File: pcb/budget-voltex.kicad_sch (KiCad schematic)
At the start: 10 parts

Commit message: put elements on pcb
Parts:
- BT-A1: renamed from BT-A; footprint (none) -> Button_Switch_Keyboard:SW_Cherry_MX_1.00u_PCB
- BT-B1: renamed from BT-B; footprint (none) -> Button_Switch_Keyboard:SW_Cherry_MX_1.00u_PCB
- BT-C1: renamed from BT-C; footprint (none) -> Button_Switch_Keyboard:SW_Cherry_MX_1.00u_PCB
- BT-D1: renamed from BT-D; footprint (none) -> Button_Switch_Keyboard:SW_Cherry_MX_1.00u_PCB
- FX-L1: renamed from FX-L; footprint (none) -> Button_Switch_Keyboard:SW_Cherry_MX_1.00u_PCB
- FX-R1: renamed from FX-R; footprint (none) -> Button_Switch_Keyboard:SW_Cherry_MX_1.00u_PCB
- Start1: renamed from Start; footprint (none) -> Button_Switch_Keyboard:SW_Cherry_MX_1.00u_PCB
- renumbered KnobL to KnobL1, KnobR to KnobR1
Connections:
- net SDA: now reaches KnobL1.1 (SCL), KnobR1.1 (SCL)
- net SDA: now also A1.1 (GPIO0)
- net SCL: now reaches KnobL1.6 (SDA), KnobR1.6 (SDA)
- net SCL: now also A1.2 (GPIO1)
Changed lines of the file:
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@@
 	(paper "A4")
+	(junction
+		(at 182.88 77.47)
+		(diameter 0)
+		(color 0 0 0 0)
+	)
 	(junction
 		(at 76.2 157.48)
@@
 	)
 	(junction
+		(at 179.07 71.12)
+		(diameter 0)
+		(color 0 0 0 0)
+	)
+	(junction
 		(at 106.68 157.48)
 		(diameter 0)
@@
 	(wire
 		(pts
+			(xy 179.07 71.12) (xy 189.23 71.12)
+		)
+		(stroke
+			(width 0)
+			(type default)
+		)
+	)
+	(wire
+		(pts
 			(xy 92.71 113.03) (xy 92.71 105.41)
 		)
@@
 	(wire
 		(pts
+			(xy 179.07 71.12) (xy 179.07 63.5)
+		)
+		(stroke
+			(width 0)
+			(type default)
+		)
+	)
+	(wire
+		(pts
 			(xy 83.82 157.48) (xy 83.82 146.05)
 		)
@@
 	(wire
 		(pts
+			(xy 182.88 77.47) (xy 182.88 66.04)
+		)
+		(stroke
+			(width 0)
+			(type default)
+		)
+	)
+	(wire
+		(pts
 			(xy 82.55 105.41) (xy 82.55 120.65)
 		)
@@
 	(wire
 		(pts
-			(xy 182.88 91.44) (xy 182.88 66.04)
+			(xy 182.88 91.44) (xy 182.88 77.47)
 		)
 		(stroke
@@
 	(wire
 		(pts
-			(xy 179.07 88.9) (xy 179.07 63.5)
+			(xy 179.07 88.9) (xy 179.07 71.12)
 		)
 		(stroke
@@
 	(wire
 		(pts
+			(xy 182.88 77.47) (xy 190.5 77.47)
+		)
+		(stroke
+			(width 0)
+			(type default)
+		)
+	)
+	(wire
+		(pts
 			(xy 100.33 115.57) (xy 90.17 115.57)
 		)
@@
 			(width 0)
 			(type default)
+		)
+	)
+	(global_label "SCL"
+		(shape input)
+		(at 74.93 105.41 270)
+		(fields_autoplaced yes)
+		(effects
+			(font
+				(size 1.27 1.27)
+			)
+			(justify right)
+		)
+		(property "Intersheetrefs" "${INTERSHEET_REFS}"
+			(at 74.93 111.9028 90)
+			(effects
+				(font
+					(size 1.27 1.27)
+				)
+				(justify right)
+				(hide yes)
+			)
+		)
+	)
+	(global_label "SCL"
+		(shape input)
+		(at 190.5 77.47 0)
+		(fields_autoplaced yes)
+		(effects
+			(font
+				(size 1.27 1.27)
+			)
+			(justify left)
+		)
+		(property "Intersheetrefs" "${INTERSHEET_REFS}"
+			(at 196.9928 77.47 0)
+			(effects
+				(font
+					(size 1.27 1.27)
+				)
+				(justify left)
+				(hide yes)
+			)
+		)
+	)
+	(global_label "SDA"
+		(shape input)
+		(at 72.39 105.41 270)
+		(fields_autoplaced yes)
+		(effects
+			(font
+				(size 1.27 1.27)
+			)
+			(justify right)
+		)
+		(property "Intersheetrefs" "${INTERSHEET_REFS}"
+			(at 72.39 111.9633 90)
+			(effects
+				(font
+					(size 1.27 1.27)
+				)
+				(justify right)
+				(hide yes)
+			)
+		)
+	)
+	(global_label "SDA"
+		(shape input)
+		(at 189.23 71.12 0)
+		(fields_autoplaced yes)
+		(effects
+			(font
+				(size 1.27 1.27)
+			)
+			(justify left)
+		)
+		(property "Intersheetrefs" "${INTERSHEET_REFS}"
+			(at 195.7833 71.12 0)
+			(effects
+				(font
+					(size 1.27 1.27)
+				)
+				(justify left)
+				(hide yes)
+			)
 		)
 	)
@@
 		(dnp no)
 		(fields_autoplaced yes)
-		(property "Reference" "KnobL"
+		(property "Reference" "KnobL1"
 			(at 158.75 53.34 0)
 			(effects
@@
 			(project "sdvx-slim"
 				(path "/f61fff6d-f3d6-4025-b479-f6b910efe925"
-					(reference "KnobL")
+					(reference "KnobL1")
 					(unit 1)
 				)
@@
 		(on_board yes)
 		(dnp no)
-		(property "Reference" "FX-L"
+		(property "Reference" "FX-L1"
 			(at 82.55 152.4 0)
 			(effects
@@
 			)
 		)
-		(property "Footprint" ""
+		(property "Footprint" "Button_Switch_Keyboard:SW_Cherry_MX_1.00u_PCB"
 			(at 76.2 152.4 0)
 			(effects
@@
 			(project "sdvx-slim"
 				(path "/f61fff6d-f3d6-4025-b479-f6b910efe925"
-					(reference "FX-L")
+					(reference "FX-L1")
 					(unit 1)
 				)
@@
 		(dnp no)
 		(fields_autoplaced yes)
-		(property "Reference" "Start"
+		(property "Reference" "Start1"
 			(at 95.25 125.7299 90)
 			(effects
@@
 			)
 		)
-		(property "Footprint" ""
+		(property "Footprint" "Button_Switch_Keyboard:SW_Cherry_MX_1.00u_PCB"
 			(at 92.71 127 0)
 			(effects
@@
 			(project "sdvx-slim"
 				(path "/f61fff6d-f3d6-4025-b479-f6b910efe925"
-					(reference "Start")
+					(reference "Start1")
 					(unit 1)
 				)
@@
 		(dnp no)
 		(fields_autoplaced yes)
-		(property "Reference" "BT-D"
+		(property "Reference" "BT-D1"
 			(at 116.84 139.6999 90)
 			(effects
@@
 			)
 		)
-		(property "Footprint" ""
+		(property "Footprint" "Button_Switch_Keyboard:SW_Cherry_MX_1.00u_PCB"
 			(at 114.3 140.97 0)
 			(effects
@@
 			(project "sdvx-slim"
 				(path "/f61fff6d-f3d6-4025-b479-f6b910efe925"
-					(reference "BT-D")
+					(reference "BT-D1")
 					(unit 1)
 				)
@@
 		(dnp no)
 		(fields_autoplaced yes)
-		(property "Reference" "KnobR"
+		(property "Reference" "KnobR1"
 			(at 158.75 78.74 0)
 			(effects
@@
 			(project ""
 				(path "/f61fff6d-f3d6-4025-b479-f6b910efe925"
-					(reference "KnobR")
+					(reference "KnobR1")
 					(unit 1)
 				)
@@
 		(dnp no)
 		(fields_autoplaced yes)
-		(property "Reference" "BT-A"
+		(property "Reference" "BT-A1"
 			(at 71.12 139.6999 90)
 			(effects
@@
 			)
 		)
-		(property "Footprint" ""
+		(property "Footprint" "Button_Switch_Keyboard:SW_Cherry_MX_1.00u_PCB"
 			(at 68.58 140.97 0)
 			(effects
@@
 			(project ""
 				(path "/f61fff6d-f3d6-4025-b479-f6b910efe925"
-					(reference "BT-A")
+					(reference "BT-A1")
 					(unit 1)
 				)
@@
 		(dnp no)
 		(fields_autoplaced yes)
-		(property "Reference" "BT-C"
+		(property "Reference" "BT-C1"
 			(at 102.87 139.6999 90)
 			(effects
@@
 			)
 		)
-		(property "Footprint" ""
+		(property "Footprint" "Button_Switch_Keyboard:SW_Cherry_MX_1.00u_PCB"
 			(at 100.33 140.97 0)
 			(effects
@@
 			(project "sdvx-slim"
 				(path "/f61fff6d-f3d6-4025-b479-f6b910efe925"
-					(reference "BT-C")
+					(reference "BT-C1")
 					(unit 1)
 				)
@@
 		(dnp no)
 		(fields_autoplaced yes)
-		(property "Reference" "BT-B"
+		(property "Reference" "BT-B1"
 			(at 86.36 139.6999 90)
 			(effects
@@
 			)
 		)
-		(property "Footprint" ""
+		(property "Footprint" "Button_Switch_Keyboard:SW_Cherry_MX_1.00u_PCB"
 			(at 83.82 140.97 0)
 			(effects
@@
 			(project "sdvx-slim"
 				(path "/f61fff6d-f3d6-4025-b479-f6b910efe925"
-					(reference "BT-B")
+					(reference "BT-B1")
 					(unit 1)
 				)
@@
 		(dnp no)
 		(fields_autoplaced yes)
-		(property "Reference" "FX-R"
+		(property "Reference" "FX-R1"
 			(at 109.22 151.1299 90)
 			(effects
@@
 			)
 		)
-		(property "Footprint" ""
+		(property "Footprint" "Button_Switch_Keyboard:SW_Cherry_MX_1.00u_PCB"
 			(at 106.68 152.4 0)
 			(effects
@@
 			(project "sdvx-slim"
 				(path "/f61fff6d-f3d6-4025-b479-f6b910efe925"
-					(reference "FX-R")
+					(reference "FX-R1")
 					(unit 1)
 				)

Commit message: finish schematic, finish wiring for pcb
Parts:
- added R1, R2, R3, R4: 5K1, Resistor_SMD:R_0603_1608Metric_Pad0.98x0.95mm_HandSolder, symbol Device:R_Small
- added USB1: HRO-TYPE-C-31-M-12, Type-C:HRO-TYPE-C-31-M-12-HandSoldering, symbol Type-C:HRO-TYPE-C-31-M-12
- A1: footprint Module:RaspberryPi_Pico_SMD_HandSolder -> Module:RaspberryPi_Pico_SMD; symbol MCU_Module:RaspberryPi_Pico_Debug -> MCU_Module:RaspberryPi_Pico_Extensive
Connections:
- net GND: now also BT-A1.2 (B), BT-B1.2 (B), BT-C1.2 (B), BT-D1.2 (B), FX-L1.2 (B), FX-R1.2 (B), Start1.2 (B), R3.2, R4.2, USB1.1 (GND), USB1.12 (GND), USB1.13 (SHIELD)
- net SCL: now also R2.2
- net SDA: now also R1.2
- net +3V3: now reaches A1.36 (3V3)
- net +3V3: now also R1.1, R2.1
- net at A1.40 (VBUS): now also USB1.11 (VBUS), USB1.2 (VBUS)
- new net: A1.TP2 (USB_DM), USB1.5 (DN2), USB1.7 (DN1)
- new net: A1.TP3 (USB_DP), USB1.6 (DP1), USB1.8 (DP2)
- new net: R3.1, USB1.4 (CC1)
- new net: R4.1, USB1.10 (CC2)
- no-connect marks 0 -> 4

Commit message: update wiring/schematic, shape pcb
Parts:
- KnobL: renamed from KnobR1; footprint DBV0006A-IPC_A -> TMAG5273A1QDBVR:DBV0006A-IPC_A
- KnobR: renamed from KnobL1; footprint DBV0006A-IPC_A -> TMAG5273A1QDBVR:DBV0006A-IPC_A
- renumbered FX-R1 to FX-L1, FX-L1 to FX-R1, Start1 to Start
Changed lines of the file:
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@@
 		(dnp no)
 		(fields_autoplaced yes)
-		(property "Reference" "KnobL1"
+		(property "Reference" "KnobR"
 			(at 158.75 53.34 0)
 			(effects
@@
 			)
 		)
-		(property "Footprint" "DBV0006A-IPC_A"
+		(property "Footprint" "TMAG5273A1QDBVR:DBV0006A-IPC_A"
 			(at 142.24 63.5 0)
 			(effects
@@
 			(project "sdvx-slim"
 				(path "/f61fff6d-f3d6-4025-b479-f6b910efe925"
-					(reference "KnobL1")
+					(reference "KnobR")
 					(unit 1)
 				)
@@
 		(on_board yes)
 		(dnp no)
-		(property "Reference" "FX-L1"
+		(property "Reference" "FX-R1"
 			(at 82.55 152.4 0)
 			(effects
@@
 			(project "sdvx-slim"
 				(path "/f61fff6d-f3d6-4025-b479-f6b910efe925"
-					(reference "FX-L1")
+					(reference "FX-R1")
 					(unit 1)
 				)
@@
 		(dnp no)
 		(fields_autoplaced yes)
-		(property "Reference" "Start1"
+		(property "Reference" "Start"
 			(at 95.25 125.7299 90)
 			(effects
@@
 			(project "sdvx-slim"
 				(path "/f61fff6d-f3d6-4025-b479-f6b910efe925"
-					(reference "Start1")
+					(reference "Start")
 					(unit 1)
 				)
@@
 		(dnp no)
 		(fields_autoplaced yes)
-		(property "Reference" "KnobR1"
+		(property "Reference" "KnobL"
 			(at 158.75 78.74 0)
 			(effects
@@
 			)
 		)
-		(property "Footprint" "DBV0006A-IPC_A"
+		(property "Footprint" "TMAG5273A1QDBVR:DBV0006A-IPC_A"
 			(at 142.24 88.9 0)
 			(effects
@@
 			(project ""
 				(path "/f61fff6d-f3d6-4025-b479-f6b910efe925"
-					(reference "KnobR1")
+					(reference "KnobL")
 					(unit 1)
 				)
@@
 		(dnp no)
 		(fields_autoplaced yes)
-		(property "Reference" "FX-R1"
+		(property "Reference" "FX-L1"
 			(at 109.22 151.1299 90)
 			(effects
@@
 			(project "sdvx-slim"
 				(path "/f61fff6d-f3d6-4025-b479-f6b910efe925"
-					(reference "FX-R1")
-					(unit 1)
-				)
+					(reference "FX-L1")
+					(unit 1)
+				)

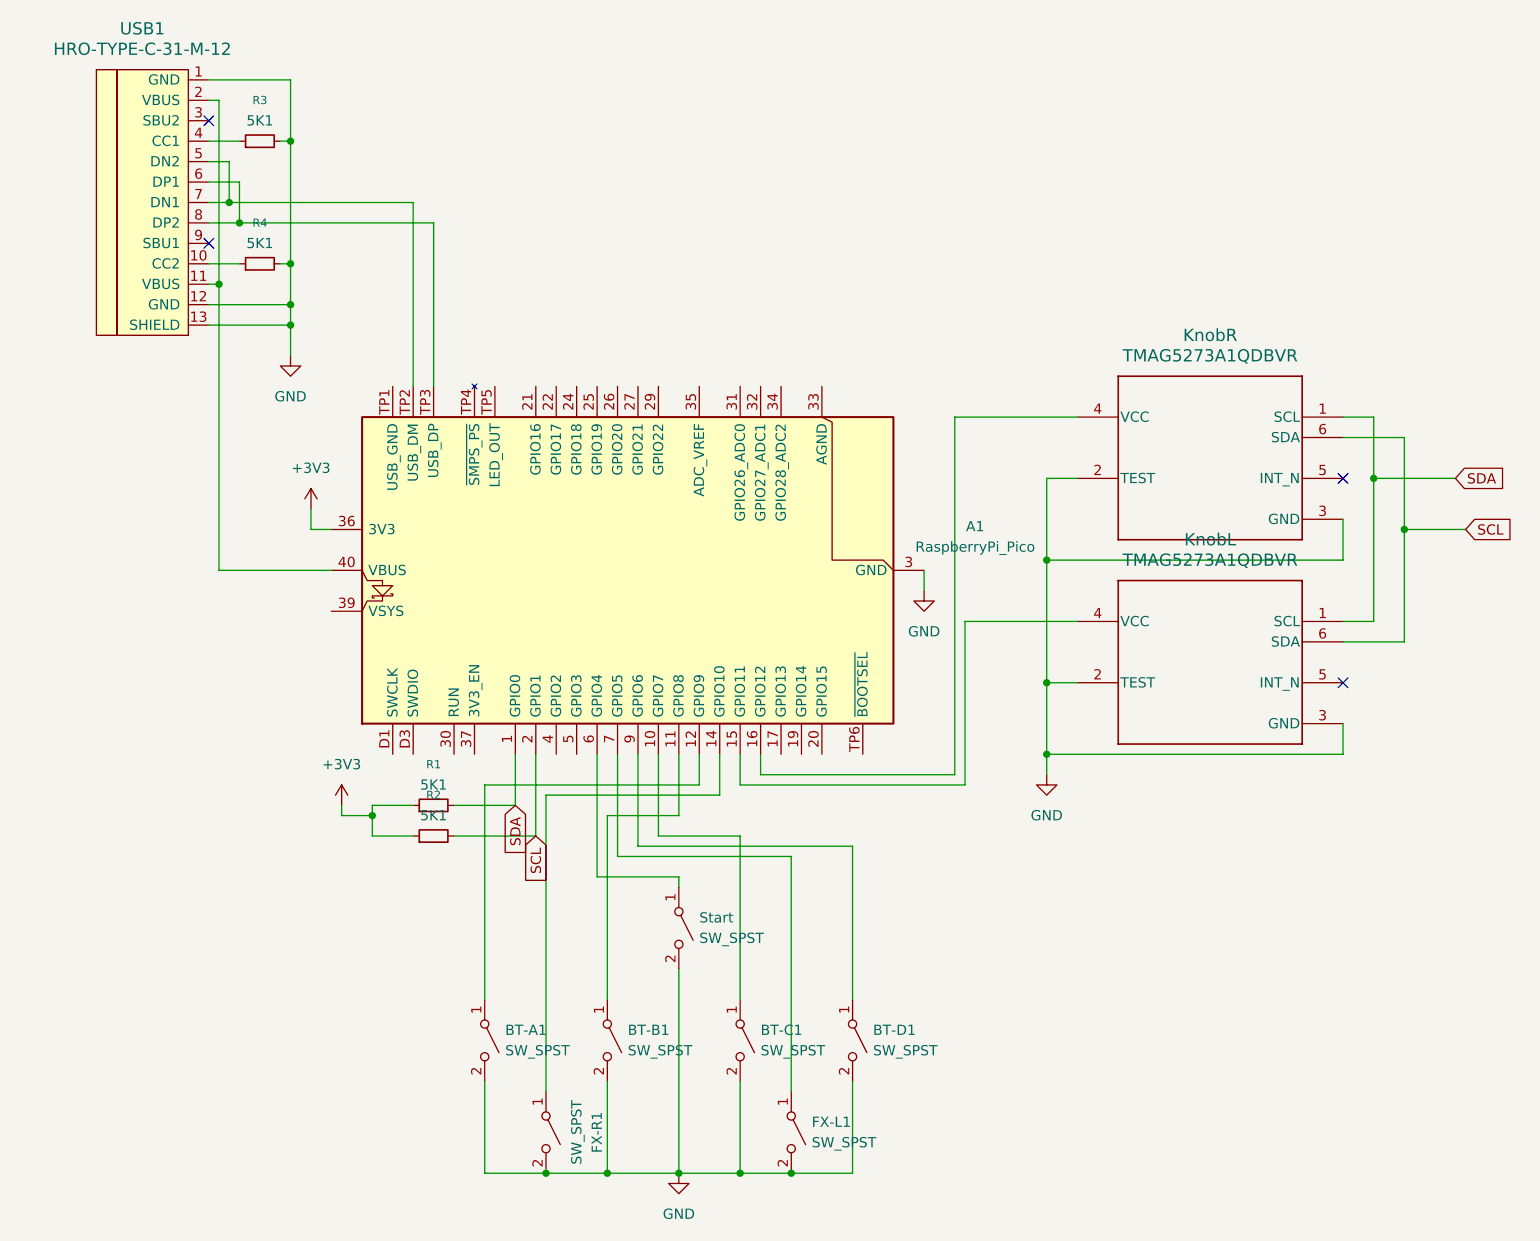
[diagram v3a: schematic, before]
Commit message: Updated key footprints to use chocs, rewire everything
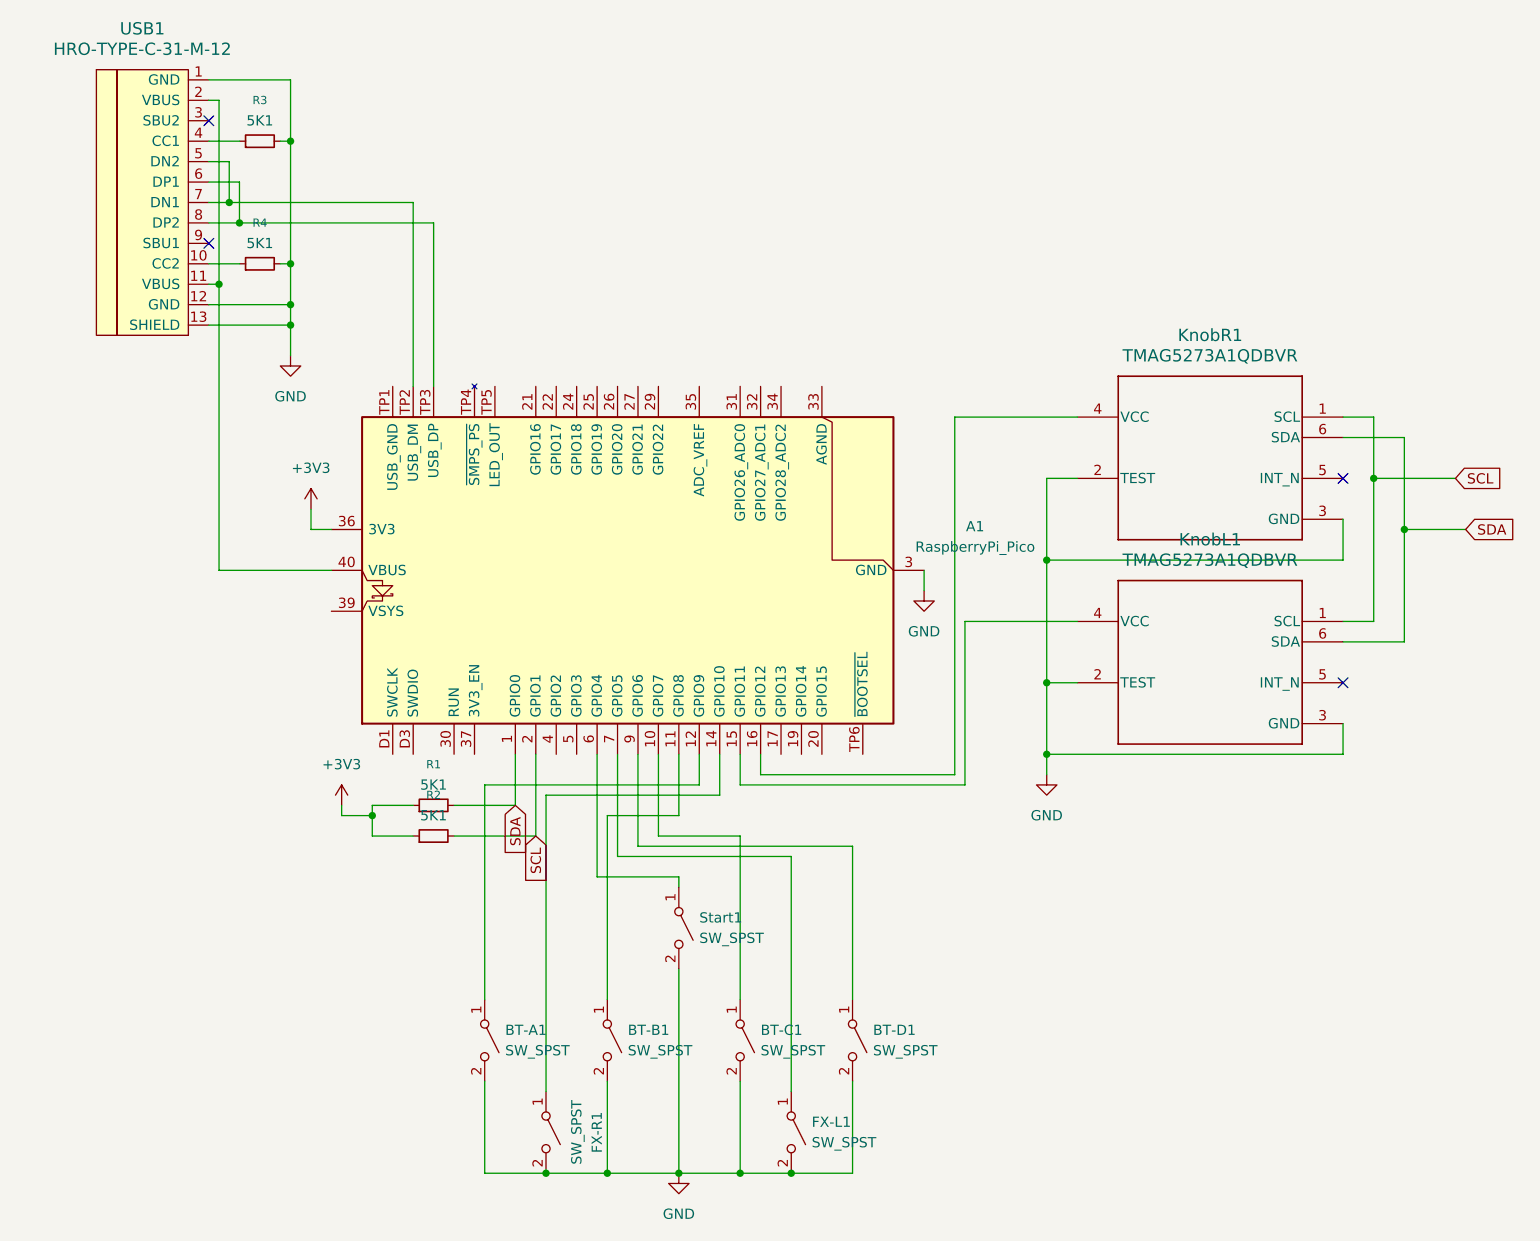
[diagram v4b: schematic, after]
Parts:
- BT-A1, BT-B1, BT-C1, BT-D1, FX-L1, FX-R1: footprint Button_Switch_Keyboard:SW_Cherry_MX_1.00u_PCB -> keyswitches:SW_PG1350
- Start1: renamed from Start; footprint Button_Switch_Keyboard:SW_Cherry_MX_1.00u_PCB -> keyswitches:SW_PG1350
- renumbered KnobL to KnobL1, KnobR to KnobR1
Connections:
- net SCL: now also KnobL1.1 (SCL), KnobR1.1 (SCL); no longer KnobL1.6 (SDA), KnobR1.6 (SDA)
- net SDA: now also KnobL1.6 (SDA), KnobR1.6 (SDA); no longer KnobL1.1 (SCL), KnobR1.1 (SCL)
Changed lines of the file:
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@@
 		)
 	)
-	(global_label "SCL"
+	(global_label "SDA"
 		(shape input)
-		(at 190.5 77.47 0)
+		(at 72.39 111.76 270)
 		(fields_autoplaced yes)
 		(effects
@@
 				(size 1.27 1.27)
 			)
-			(justify left)
+			(justify right)
 		)
 		(property "Intersheetrefs" "${INTERSHEET_REFS}"
-			(at 196.9928 77.47 0)
-			(effects
-				(font
-					(size 1.27 1.27)
-				)
-				(justify left)
-				(hide yes)
-			)
-		)
-	)
-	(global_label "SDA"
+			(at 72.39 118.3133 90)
+			(effects
+				(font
+					(size 1.27 1.27)
+				)
+				(justify right)
+				(hide yes)
+			)
+		)
+	)
+	(global_label "SCL"
 		(shape input)
-		(at 72.39 111.76 270)
+		(at 189.23 71.12 0)
 		(fields_autoplaced yes)
 		(effects
@@
 				(size 1.27 1.27)
 			)
-			(justify right)
+			(justify left)
 		)
 		(property "Intersheetrefs" "${INTERSHEET_REFS}"
-			(at 72.39 118.3133 90)
-			(effects
-				(font
-					(size 1.27 1.27)
-				)
-				(justify right)
+			(at 195.7228 71.12 0)
+			(effects
+				(font
+					(size 1.27 1.27)
+				)
+				(justify left)
 				(hide yes)
 			)
@@
 	(global_label "SDA"
 		(shape input)
-		(at 189.23 71.12 0)
+		(at 190.5 77.47 0)
 		(fields_autoplaced yes)
 		(effects
@@
 		)
 		(property "Intersheetrefs" "${INTERSHEET_REFS}"
-			(at 195.7833 71.12 0)
+			(at 197.0533 77.47 0)
 			(effects
 				(font
@@
 		(dnp no)
 		(fields_autoplaced yes)
-		(property "Reference" "KnobR"
+		(property "Reference" "KnobR1"
 			(at 158.75 53.34 0)
 			(effects
@@
 			(project "sdvx-slim"
 				(path "/f61fff6d-f3d6-4025-b479-f6b910efe925"
-					(reference "KnobR")
+					(reference "KnobR1")
 					(unit 1)
 				)
@@
 			)
 		)
-		(property "Footprint" "Button_Switch_Keyboard:SW_Cherry_MX_1.00u_PCB"
+		(property "Footprint" "keyswitches:SW_PG1350"
 			(at 76.2 152.4 0)
 			(effects
@@
 		(dnp no)
 		(fields_autoplaced yes)
-		(property "Reference" "Start"
+		(property "Reference" "Start1"
 			(at 95.25 125.7299 90)
 			(effects
@@
 			)
 		)
-		(property "Footprint" "Button_Switch_Keyboard:SW_Cherry_MX_1.00u_PCB"
+		(property "Footprint" "keyswitches:SW_PG1350"
 			(at 92.71 127 0)
 			(effects
@@
 			(project "sdvx-slim"
 				(path "/f61fff6d-f3d6-4025-b479-f6b910efe925"
-					(reference "Start")
+					(reference "Start1")
 					(unit 1)
 				)
@@
 			)
 		)
-		(property "Footprint" "Button_Switch_Keyboard:SW_Cherry_MX_1.00u_PCB"
+		(property "Footprint" "keyswitches:SW_PG1350"
 			(at 114.3 140.97 0)
 			(effects
@@
 		(dnp no)
 		(fields_autoplaced yes)
-		(property "Reference" "KnobL"
+		(property "Reference" "KnobL1"
 			(at 158.75 78.74 0)
 			(effects
@@
 			(project ""
 				(path "/f61fff6d-f3d6-4025-b479-f6b910efe925"
-					(reference "KnobL")
+					(reference "KnobL1")
 					(unit 1)
 				)
@@
 			)
 		)
-		(property "Footprint" "Button_Switch_Keyboard:SW_Cherry_MX_1.00u_PCB"
+		(property "Footprint" "keyswitches:SW_PG1350"
 			(at 68.58 140.97 0)
 			(effects
@@
 			)
 		)
-		(property "Footprint" "Button_Switch_Keyboard:SW_Cherry_MX_1.00u_PCB"
+		(property "Footprint" "keyswitches:SW_PG1350"
 			(at 100.33 140.97 0)
 			(effects
@@
 			)
 		)
-		(property "Footprint" "Button_Switch_Keyboard:SW_Cherry_MX_1.00u_PCB"
+		(property "Footprint" "keyswitches:SW_PG1350"
 			(at 83.82 140.97 0)
 			(effects
@@
 			)
 		)
-		(property "Footprint" "Button_Switch_Keyboard:SW_Cherry_MX_1.00u_PCB"
+		(property "Footprint" "keyswitches:SW_PG1350"
 			(at 106.68 152.4 0)
 			(effects

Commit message: Idk what i did
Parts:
- A1: footprint Module:RaspberryPi_Pico_SMD -> minnowfeather-custom-fp:RaspberryPi_Pico_SMD_Modified
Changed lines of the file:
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@@
 			)
 		)
-		(property "Footprint" "Module:RaspberryPi_Pico_SMD"
+		(property "Footprint" "minnowfeather-custom-fp:RaspberryPi_Pico_SMD_Modified"
 			(at 134.62 82.55 0)
 			(effects
